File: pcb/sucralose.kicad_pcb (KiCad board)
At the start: 2 copper layers, 141.8 x 89.9 mm, 70 parts, among them M1 MountingHole_1.2mm_M1

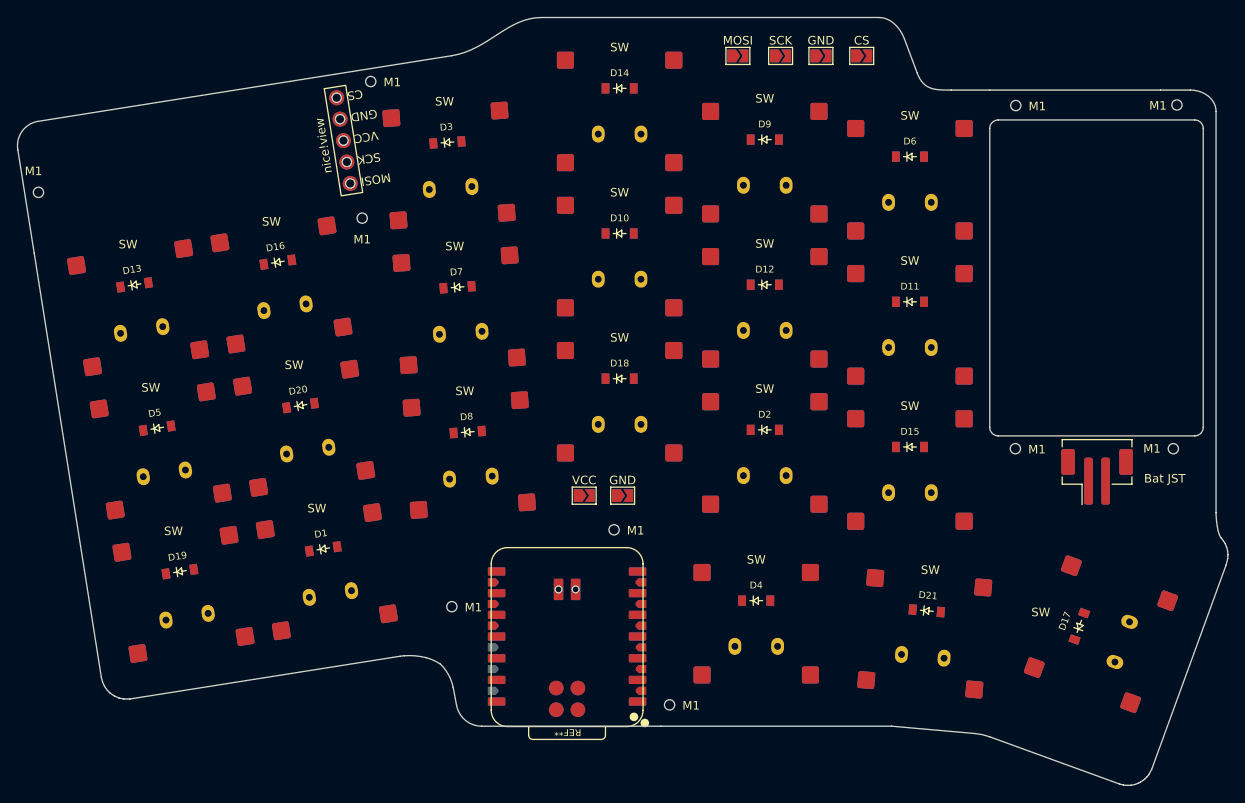
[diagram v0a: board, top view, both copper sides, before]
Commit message: Route all 43 nets: 506 segments, 86 vias, zero copper errors
Scripted grid A* router (scripts/route/). No autorouter exists in the
container: kicad-cli has no DSN export and there is no Java.

Routed on 0.25 mm grid, 0.25 mm track, 0.3 mm clearance (netclass 0.2),
0.6/0.3 vias. Rows prefer B.Cu, columns F.Cu. Every net reached every
site: 0 router failures.

DRC after routing:
  shorting_items      0
  clearance           0
  hole_clearance      0
  track_dangling      0
  unconnected_items  20 (was 138)
  everything else unchanged at the 88 pre-routing baseline

Three bugs fixed on the way, each caught by kicad-cli DRC not by the router:
  * snapping a segment endpoint to the pad centre dragged the whole segment
    off its A*-verified cells and through a neighbouring diode pad (2 shorts
    on COL1). Now a separate short stub is added instead.
  * ring pads over the NPTH barrels were entered at the centre = the drill.
    Now entry cells exclude the barrel + hole clearance, and no snap.
  * back-face SMD lands of front-mounted parts were usable as terminals, so
    tracks ended on unpopulated copper islands (35 dangling). Now they are
    hard obstacles.

Remaining 20 unconnected, all at the jumper strips and reversible rings,
documented in the next commit message / chat.
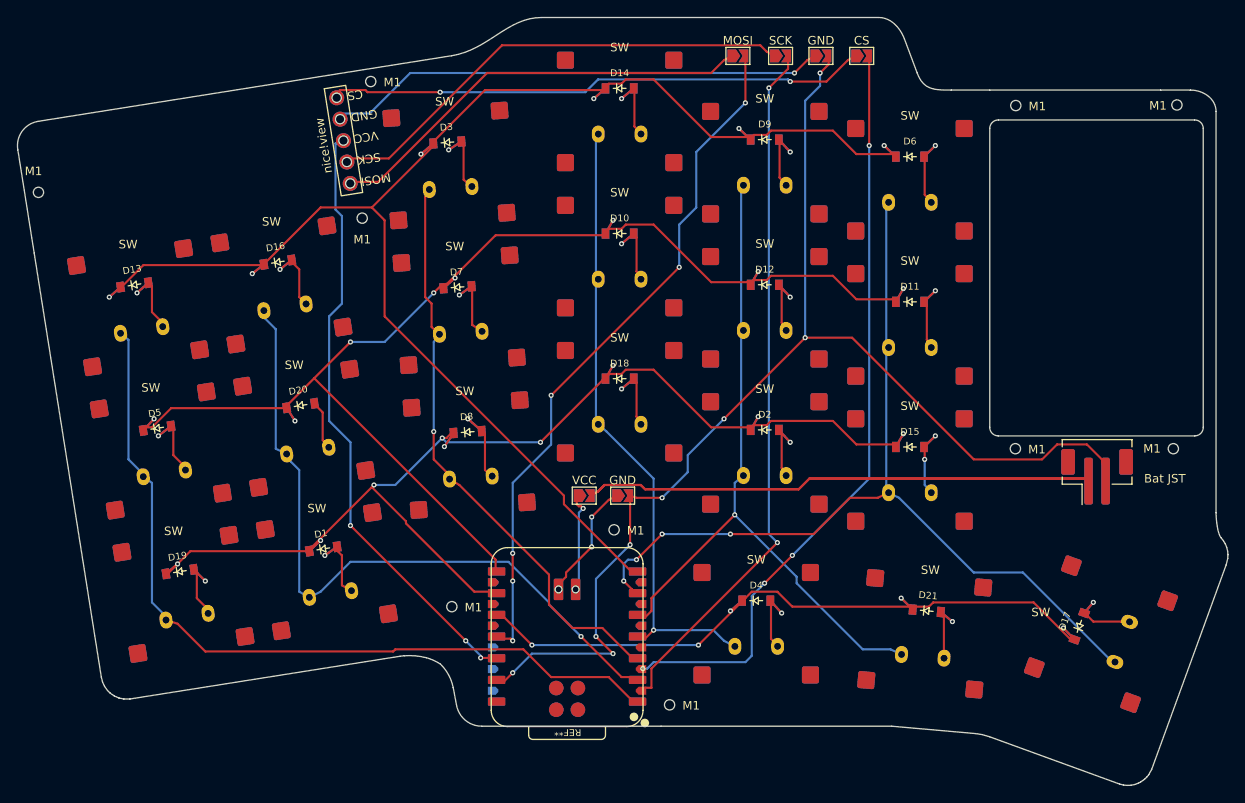
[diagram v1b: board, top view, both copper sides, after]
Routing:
- net ROW0: track 0.00 -> 183.7 mm, vias 0 -> 6
- net ROW1: track 0.00 -> 156.2 mm, vias 0 -> 8
- net GND: track 0.00 -> 144.5 mm, vias 0 -> 8
- net ROW2: track 0.00 -> 143.6 mm, vias 0 -> 9
- net BAT_P: track 0.00 -> 119.2 mm
- net COL5: track 0.00 -> 107.3 mm, vias 0 -> 4
- net COL0: track 0.00 -> 95.0 mm
- net CS: track 0.00 -> 89.8 mm, vias 0 -> 4
- net ROW3: track 0.00 -> 85.8 mm, vias 0 -> 5
- net COL4: track 0.00 -> 83.1 mm, vias 0 -> 1
- net SCK: track 0.00 -> 82.8 mm, vias 0 -> 2
- net COL1: track 0.00 -> 82.0 mm, vias 0 -> 1
- net MOSI: track 0.00 -> 81.8 mm, vias 0 -> 6
- net COL3: track 0.00 -> 73.5 mm, vias 0 -> 1
- net VCC: track 0.00 -> 70.7 mm, vias 0 -> 3
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
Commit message: Netlist for both builds; strip copper pending jumper-strip respacing
The back XIAO's signal pads (1-13, 15, 16) and the back JST are real
terminals for the reverse build, not dead copper. Net them:
  back XIAO pad N = front XIAO pad N (same GPIO), 15 pads
  back JST 1=GND 2=BAT_P (mirror of front 1=BAT_P 2=GND)
Battery lands 28/29 stay per-hole and swap on mirror, as before.

Copper removed. The front-only route in 2b59dac was built on the wrong
model (back lands as obstacles). Routing both builds against the
current geometry fails on 3 nets after rip-up: every signal must reach
both mirrored XIAO pad rows through the same ~13 mm of edge, and the
jumper strip at y=53.5 has ~5 mm pitch with no lane between pads.
Next: user respaces the jumper strip; router allows vias under the XIAO.

scripts/route: grid 0.125 mm, geometric clearance halos, search cap,
rip-up driver (drive2.py). audit_netlist.py now checks back XIAO pads
match front, not that they are empty.
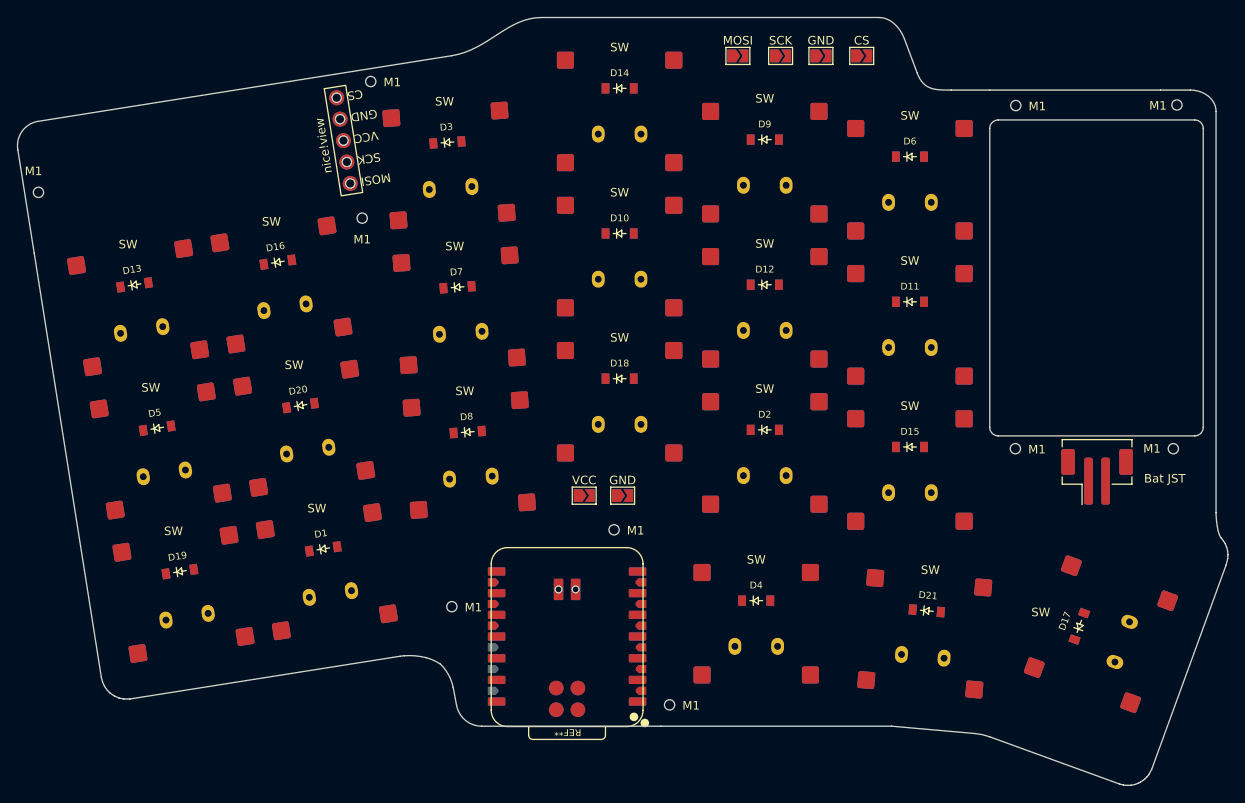
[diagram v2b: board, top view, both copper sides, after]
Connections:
- Bat JST pad 1: (no net) -> GND
- Bat JST pad 2: (no net) -> BAT_P
- REF** pad 1: (no net) -> COL0
- REF** pad 10: (no net) -> ROW3
- REF** pad 11: (no net) -> MOSI
- REF** pad 12: (no net) -> VCC
- REF** pad 13: (no net) -> GND
- REF** pad 15: (no net) -> SCK
- REF** pad 16: (no net) -> CS
- REF** pad 2: (no net) -> COL1
- REF** pad 3: (no net) -> COL2
- REF** pad 4: (no net) -> COL3
- REF** pad 5: (no net) -> COL4
- REF** pad 6: (no net) -> COL5
- REF** pad 7: (no net) -> ROW0
- REF** pad 8: (no net) -> ROW1
- REF** pad 9: (no net) -> ROW2
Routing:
- net ROW0: track 183.7 -> 0.00 mm, vias 6 -> 0
- net ROW1: track 156.2 -> 0.00 mm, vias 8 -> 0
- net GND: track 144.5 -> 0.00 mm, vias 8 -> 0
- net ROW2: track 143.6 -> 0.00 mm, vias 9 -> 0
- net BAT_P: track 119.2 -> 0.00 mm
- net COL5: track 107.3 -> 0.00 mm, vias 4 -> 0
- net COL0: track 95.0 -> 0.00 mm
- net CS: track 89.8 -> 0.00 mm, vias 4 -> 0
- net ROW3: track 85.8 -> 0.00 mm, vias 5 -> 0
- net COL4: track 83.1 -> 0.00 mm, vias 1 -> 0
- net SCK: track 82.8 -> 0.00 mm, vias 2 -> 0
- net COL1: track 82.0 -> 0.00 mm, vias 1 -> 0
- net MOSI: track 81.8 -> 0.00 mm, vias 6 -> 0
- net COL3: track 73.5 -> 0.00 mm, vias 1 -> 0
- net VCC: track 70.7 -> 0.00 mm, vias 3 -> 0
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
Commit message: Moved display jumpers and GND jumper to give routing space.
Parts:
- moved GND 4.28 mm to (138.3, 105.0) (x2)
- moved MOSI 3.22 mm to (144.3, 53.5) (x2)
- moved SCK 1.72 mm to (150.8, 53.5) (x2)
- moved CS 1.50 mm to (163.5, 53.5) (x2)
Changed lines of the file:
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@@
 	(footprint "Jumper:SolderJumper-2_P1.3mm_Open_TrianglePad1.0x1.5mm"
 		(layer "F.Cu")
-		(at 152.5 53.5)
+		(at 150.775 53.5)
 		(descr "SMD Solder Jumper, 1x1.5mm Triangular Pads, 0.3mm gap, open")
 		(tags "solder jumper open")
@@
 	(footprint "Jumper:SolderJumper-2_P1.3mm_Open_TrianglePad1.0x1.5mm"
 		(layer "F.Cu")
-		(at 162 53.5)
+		(at 163.5 53.5)
 		(descr "SMD Solder Jumper, 1x1.5mm Triangular Pads, 0.3mm gap, open")
 		(tags "solder jumper open")
@@
 	(footprint "Jumper:SolderJumper-2_P1.3mm_Open_TrianglePad1.0x1.5mm"
 		(layer "F.Cu")
-		(at 134 105)
+		(at 138.275 105)
 		(descr "SMD Solder Jumper, 1x1.5mm Triangular Pads, 0.3mm gap, open")
 		(tags "solder jumper open")
@@
 	(footprint "Jumper:SolderJumper-2_P1.3mm_Open_TrianglePad1.0x1.5mm"
 		(layer "F.Cu")
-		(at 147.5 53.5)
+		(at 144.275659 53.5)
 		(descr "SMD Solder Jumper, 1x1.5mm Triangular Pads, 0.3mm gap, open")
 		(tags "solder jumper open")
@@
 			(layers "B.Cu" "B.Mask" "B.Paste")
 			(roundrect_rratio 0.1)
-			(thermal_bridge_angle 45)
 			(net "COL0")
+			(thermal_bridge_angle 45)
 		)
 		(pad "2" smd roundrect
@@
 			(layers "B.Cu" "B.Mask" "B.Paste")
 			(roundrect_rratio 0.1)
-			(thermal_bridge_angle 45)
 			(net "COL1")
+			(thermal_bridge_angle 45)
 		)
 		(pad "3" smd roundrect
@@
 			(layers "B.Cu" "B.Mask" "B.Paste")
 			(roundrect_rratio 0.1)
-			(thermal_bridge_angle 45)
 			(net "COL2")
+			(thermal_bridge_angle 45)
 		)
 		(pad "4" smd roundrect
@@
 			(layers "B.Cu" "B.Mask" "B.Paste")
 			(roundrect_rratio 0.1)
-			(thermal_bridge_angle 45)
 			(net "COL3")
+			(thermal_bridge_angle 45)
 		)
 		(pad "5" smd roundrect
@@
 			(layers "B.Cu" "B.Mask" "B.Paste")
 			(roundrect_rratio 0.1)
-			(thermal_bridge_angle 45)
 			(net "COL4")
+			(thermal_bridge_angle 45)
 		)
 		(pad "6" smd roundrect
@@
 			(layers "B.Cu" "B.Mask" "B.Paste")
 			(roundrect_rratio 0.1)
-			(thermal_bridge_angle 45)
 			(net "COL5")
+			(thermal_bridge_angle 45)
 		)
 		(pad "7" smd roundrect
@@
 			(layers "B.Cu" "B.Mask" "B.Paste")
 			(roundrect_rratio 0.1)
-			(thermal_bridge_angle 45)
 			(net "ROW0")
+			(thermal_bridge_angle 45)
 		)
 		(pad "8" smd roundrect
@@
 			(layers "B.Cu" "B.Mask" "B.Paste")
 			(roundrect_rratio 0.1)
-			(thermal_bridge_angle 45)
 			(net "ROW1")
+			(thermal_bridge_angle 45)
 		)
 		(pad "9" smd roundrect
@@
 			(layers "B.Cu" "B.Mask" "B.Paste")
 			(roundrect_rratio 0.1)
-			(thermal_bridge_angle 45)
 			(net "ROW2")
+			(thermal_bridge_angle 45)
 		)
 		(pad "10" smd roundrect
@@
 			(layers "B.Cu" "B.Mask" "B.Paste")
 			(roundrect_rratio 0.1)
-			(thermal_bridge_angle 45)
 			(net "ROW3")
+			(thermal_bridge_angle 45)
 		)
 		(pad "11" smd roundrect
@@
 			(layers "B.Cu" "B.Mask" "B.Paste")
 			(roundrect_rratio 0.1)
-			(thermal_bridge_angle 45)
 			(net "MOSI")
+			(thermal_bridge_angle 45)
 		)
 		(pad "12" smd roundrect
@@
 			(layers "B.Cu" "B.Mask" "B.Paste")
 			(roundrect_rratio 0.1)
-			(thermal_bridge_angle 45)
 			(net "VCC")
+			(thermal_bridge_angle 45)
 		)
 		(pad "13" smd roundrect
@@
 			(layers "B.Cu" "B.Mask" "B.Paste")
 			(roundrect_rratio 0.1)
-			(thermal_bridge_angle 45)
 			(net "GND")
+			(thermal_bridge_angle 45)
 		)
 		(pad "14" smd roundrect
@@
 			(chamfer_ratio 0.35)
 			(chamfer top_left bottom_left)
-			(thermal_bridge_angle 45)
 			(net "SCK")
+			(thermal_bridge_angle 45)
 		)
 		(pad "16" smd roundrect
@@
 			(chamfer_ratio 0.35)
 			(chamfer top_left bottom_left)
-			(thermal_bridge_angle 45)
 			(net "CS")
+			(thermal_bridge_angle 45)
 		)
 		(pad "17" smd roundrect
@@
 	(footprint "Jumper:SolderJumper-2_P1.3mm_Open_TrianglePad1.0x1.5mm"
 		(layer "B.Cu")
-		(at 152.499341 53.495232)
+		(at 150.774341 53.495232)
 		(descr "SMD Solder Jumper, 1x1.5mm Triangular Pads, 0.3mm gap, open")
 		(tags "solder jumper open")
@@
 	(footprint "Jumper:SolderJumper-2_P1.3mm_Open_TrianglePad1.0x1.5mm"
 		(layer "B.Cu")
-		(at 134.005498 104.994199)
+		(at 138.280498 104.994199)
 		(descr "SMD Solder Jumper, 1x1.5mm Triangular Pads, 0.3mm gap, open")
 		(tags "solder jumper open")
@@
 	(footprint "Jumper:SolderJumper-2_P1.3mm_Open_TrianglePad1.0x1.5mm"
 		(layer "B.Cu")
-		(at 147.499341 53.495232)
+		(at 144.275 53.495232)
 		(descr "SMD Solder Jumper, 1x1.5mm Triangular Pads, 0.3mm gap, open")
 		(tags "solder jumper open")
@@
 	(footprint "Jumper:SolderJumper-2_P1.3mm_Open_TrianglePad1.0x1.5mm"
 		(layer "B.Cu")
-		(at 161.999341 53.495232)
+		(at 163.499341 53.495232)
 		(descr "SMD Solder Jumper, 1x1.5mm Triangular Pads, 0.3mm gap, open")
 		(tags "solder jumper open")
